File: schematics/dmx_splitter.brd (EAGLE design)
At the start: 101.7 x 55.9 mm, 39 parts

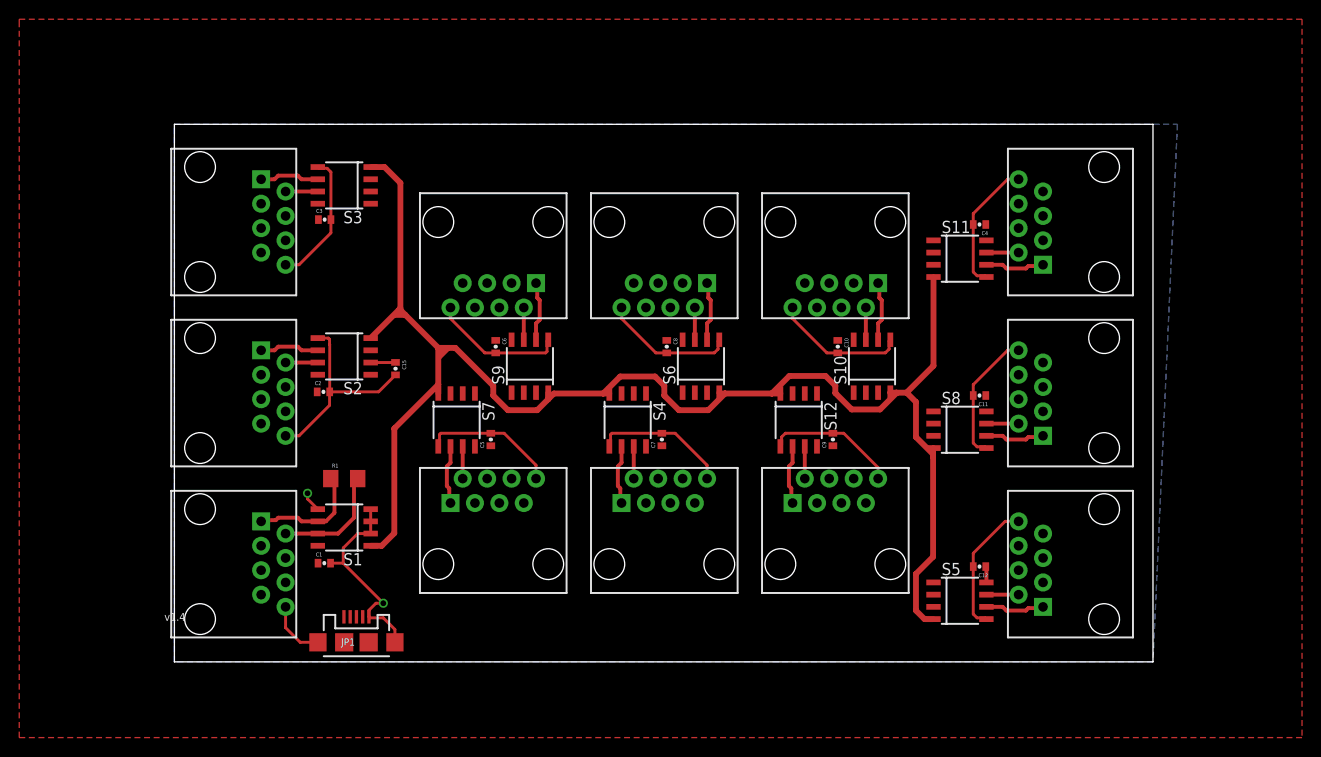
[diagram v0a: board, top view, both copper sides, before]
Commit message: made board 10cm wide
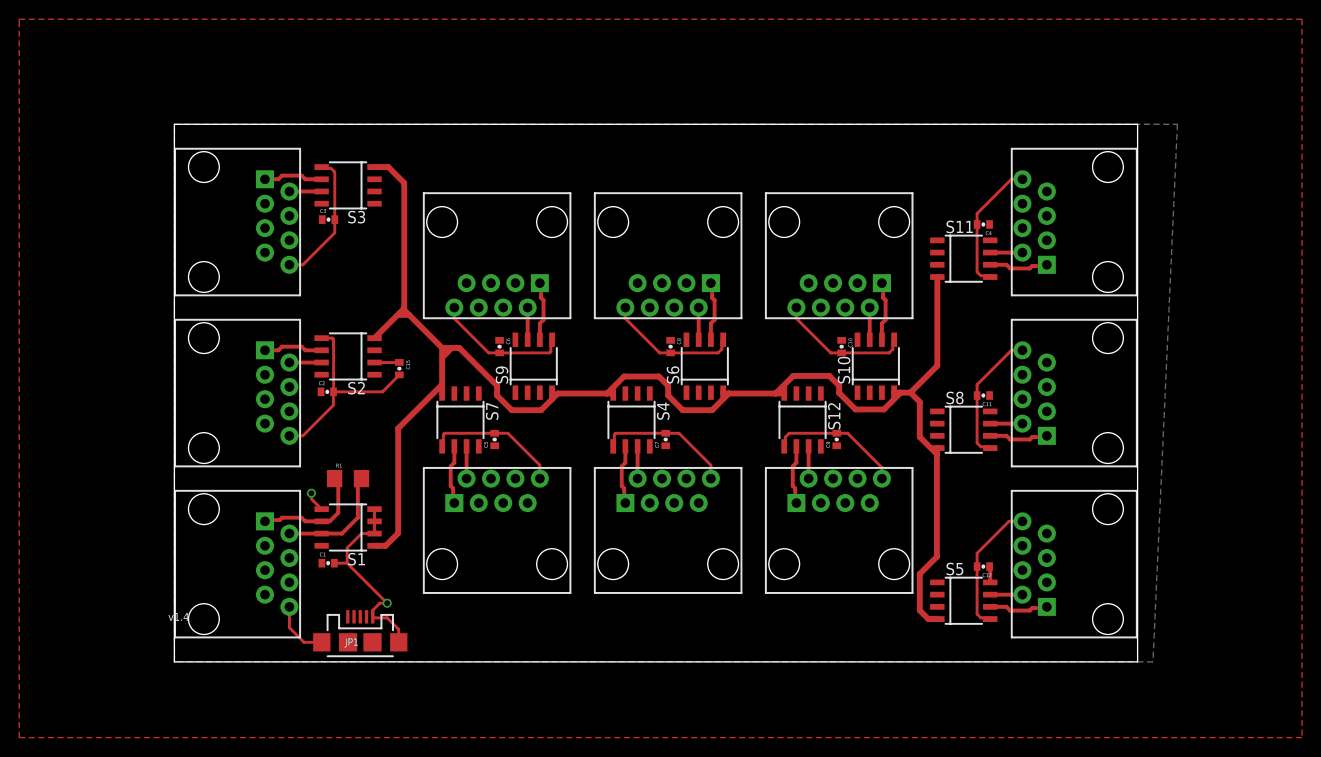
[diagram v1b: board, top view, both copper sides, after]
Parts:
- moved C9 0.40 mm to (68.7, 23.1)
- moved E10 0.40 mm to (69.0, 45.7)
- moved E11 0.40 mm to (96.9, 45.7)
- moved E12 0.40 mm to (69.0, 10.2)
- moved E4 0.40 mm to (51.2, 10.2)
- moved E5 0.40 mm to (96.9, 10.2)
- moved E6 0.40 mm to (51.2, 45.7)
- moved E8 0.40 mm to (96.9, 27.9)
- moved S10 0.40 mm to (72.8, 30.7)
- moved S12 0.40 mm to (65.2, 25.1)
- moved C15 0.40 mm to (23.3, 30.5)
- moved JP1 0.40 mm to (19.2, 2.03)
- moved C1 0.40 mm to (15.9, 10.3)
- moved C3 0.40 mm to (15.9, 46.0)
- moved E1 0.40 mm to (2.94, 10.2)
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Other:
- board size 101.7 x 55.9 mm -> 100.1 x 55.9 mm

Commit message: Remove negative offset on board edge...
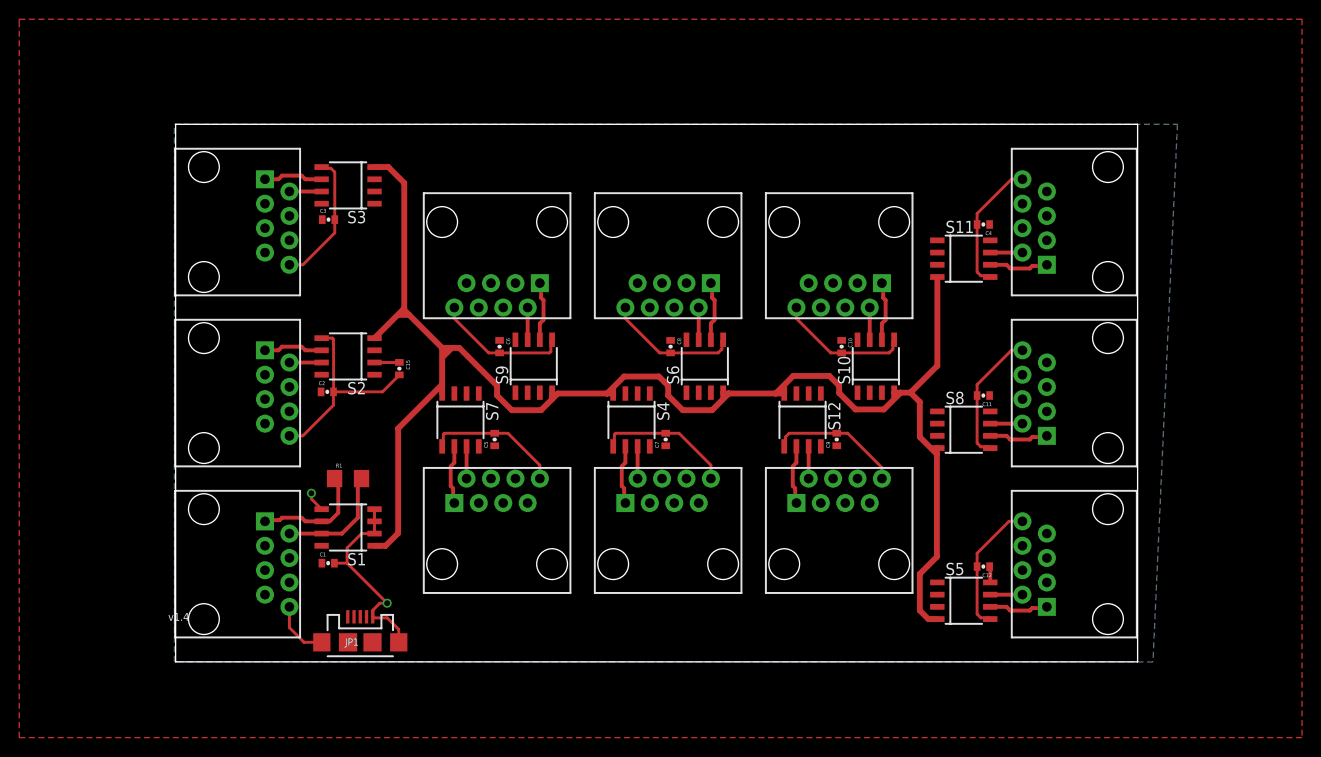
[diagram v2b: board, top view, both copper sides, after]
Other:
- board size 100.1 x 55.9 mm -> 100 x 55.9 mm
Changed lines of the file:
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@@
 <?xml version="1.0" encoding="utf-8"?>
 <!DOCTYPE eagle SYSTEM "eagle.dtd">
-<eagle version="6.3">
+<eagle version="6.4">
 <drawing>
 <settings>
@@
 <board>
 <plain>
-<wire x1="-0.127" y1="0" x2="100" y2="0" width="0" layer="20"/>
+<wire x1="0" y1="0" x2="100" y2="0" width="0" layer="20"/>
 <wire x1="100" y1="0" x2="100" y2="55.88" width="0" layer="20"/>
-<wire x1="100" y1="55.88" x2="-0.127" y2="55.88" width="0" layer="20"/>
-<wire x1="-0.127" y1="55.88" x2="-0.127" y2="0" width="0" layer="20"/>
+<wire x1="100" y1="55.88" x2="0" y2="55.88" width="0" layer="20"/>
+<wire x1="0" y1="55.88" x2="0" y2="0" width="0" layer="20"/>
 <text x="1.416" y="5.08" size="0.8128" layer="21" distance="213" align="top-right">v1.4</text>
 </plain>
